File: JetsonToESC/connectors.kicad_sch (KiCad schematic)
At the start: 7 parts, among them J1 Conn_01x12, J2 Conn_01x03, J3 Conn_01x02

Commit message: Start On this Branch
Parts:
- added U4: MCP23018x-x-SS, Package_SO:SSOP-24_5.3x8.2mm_P0.65mm, symbol Interface_Expansion:MCP23018x-x-SS
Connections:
- net 5V: now also U4.10 (V_{DD})
- net BUTTON_100%: now also U4.22 (GPA5)
- net BUTTON_25%: now also U4.19 (GPA2)
- net BUTTON_50%: now also U4.20 (GPA3)
- net BUTTON_75%: now also U4.21 (GPA4)
- net BUTTON_STOP: now also U4.18 (GPA1)
- net GND: now also U4.1 (V_{SS})
- net LED_BATT_HI: now also U4.7 (GPB5)
- net LED_BATT_LOW: now also U4.9 (GPB7)
- net LED_BATT_MED: now also U4.8 (GPB6)
- net LED_OVERCURRENT: now also U4.5 (GPB3), U4.6 (GPB4)
- new net I2C_SCL: U4.11 (SCL)
- new net I2C_SDA: U4.12 (SDA)
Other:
- moved on the sheet: H1, H2, H3, H4, J1, J2, J3

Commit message: Work on current sense and io expansion branch
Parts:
- removed U4: MCP23018x-x-SS, Package_SO:SSOP-24_5.3x8.2mm_P0.65mm, symbol Interface_Expansion:MCP23018x-x-SS
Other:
- moved on the sheet: J1, J2, J3

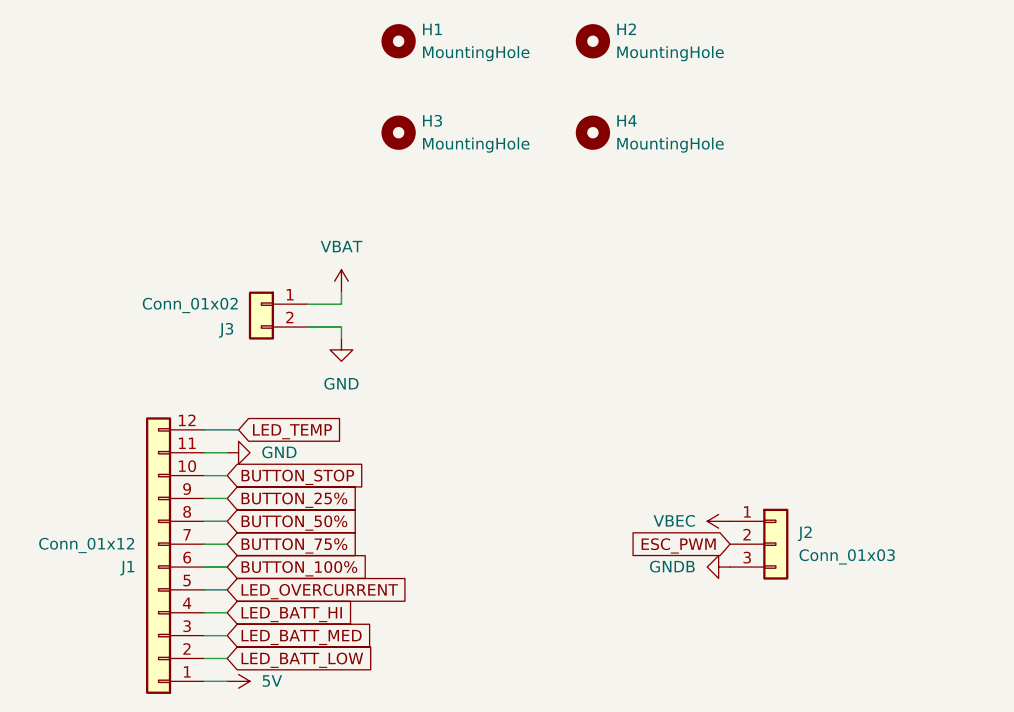
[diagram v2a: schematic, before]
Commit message: Updated routing for IO Expander and Hall Sensor
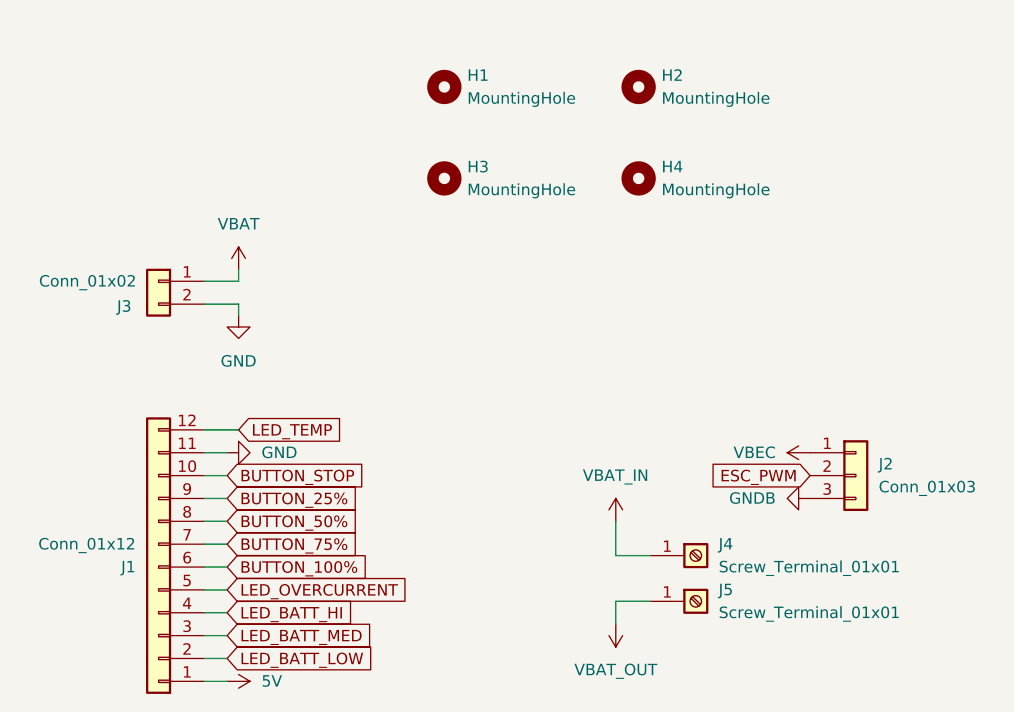
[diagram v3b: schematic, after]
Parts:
- added J4, J5: Screw_Terminal_01x01, MountingHole:MountingHole_4.3mm_M4_Pad_Via, symbol Connector:Screw_Terminal_01x01
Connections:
- new net VBAT_IN: J4.1 (Pin_1)
- new net VBAT_OUT: J5.1 (Pin_1)
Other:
- moved on the sheet: H1, H2, H3, H4, J2, J3

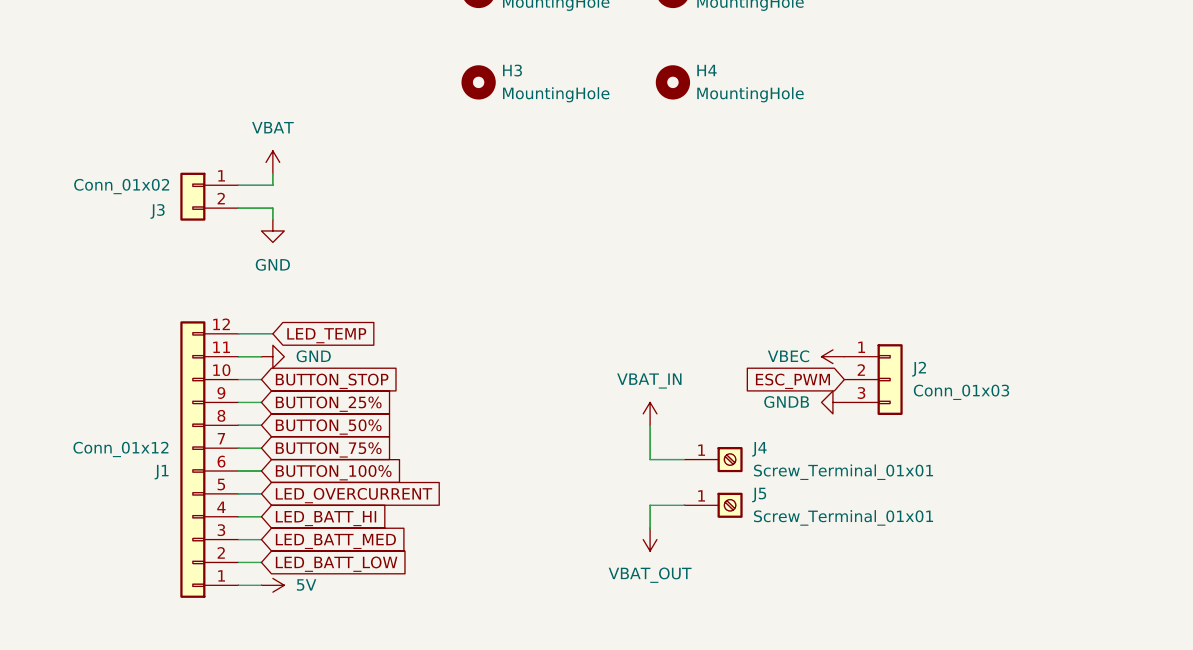
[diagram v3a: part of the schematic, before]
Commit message: Design almost finished, added vias array for grounding too
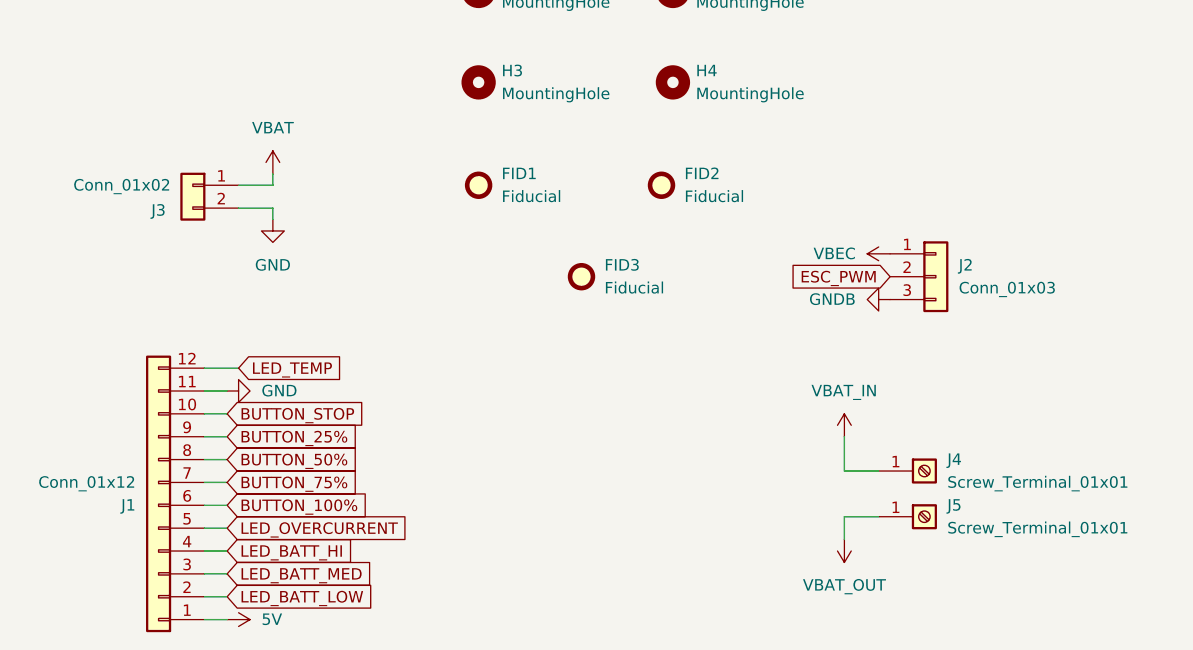
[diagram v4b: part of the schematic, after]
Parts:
- added FID1, FID2, FID3: Fiducial, Fiducial:Fiducial_0.5mm_Mask1.5mm, symbol Mechanical:Fiducial
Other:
- moved on the sheet: J1, J2, J4, J5

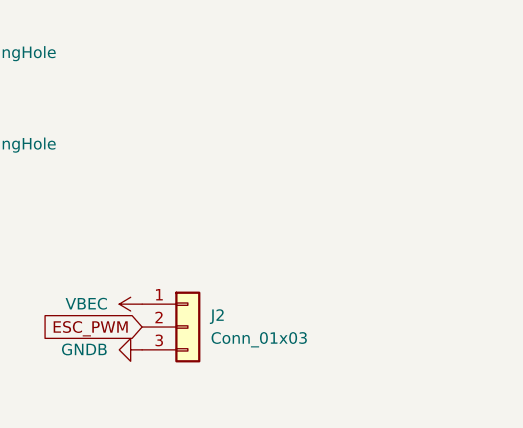
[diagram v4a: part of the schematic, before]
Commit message: Design almost finished, added vias array for grounding too
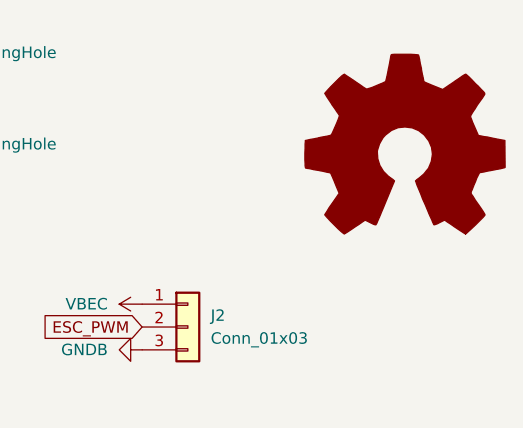
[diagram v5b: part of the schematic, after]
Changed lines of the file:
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@@
+	)
+	(symbol
+		(lib_id "Graphic:Logo_Open_Hardware_Large")
+		(at 170.18 36.83 0)
+		(unit 1)
+		(exclude_from_sim no)
+		(in_bom no)
+		(on_board no)
+		(dnp no)
+		(fields_autoplaced yes)
+		(property "Reference" "#SYM1"
+			(at 170.18 24.13 0)
+			(effects
+				(font
+					(size 1.27 1.27)
+				)
+				(hide yes)
+			)
+		)
+		(property "Value" "Logo_Open_Hardware_Large"
+			(at 170.18 46.99 0)
+			(effects
+				(font
+					(size 1.27 1.27)
+				)
+				(hide yes)
+			)
+		)
+		(property "Footprint" "Symbol:OSHW-Logo_28.5x30mm_SilkScreen"
+			(at 170.18 36.83 0)
+			(effects
+				(font
+					(size 1.27 1.27)
+				)
+				(hide yes)
+			)
+		)
+		(property "Datasheet" "~"
+			(at 170.18 36.83 0)
+			(effects
+				(font
+					(size 1.27 1.27)
+				)
+				(hide yes)
+			)
+		)
+		(property "Description" "Open Hardware logo, large"
+			(at 170.18 36.83 0)
+			(effects
+				(font
+					(size 1.27 1.27)
+				)
+				(hide yes)
+			)
+		)
+		(property "Sim.Enable" "0"
+			(at 170.18 36.83 0)
+			(effects
+				(font
+					(size 1.27 1.27)
+				)
+				(hide yes)
+			)
+		)
+		(instances
+			(project ""
+				(path "/47af999a-55f7-4333-ac4c-b272b7fb2895/bd87f1de-e46c-4816-9460-8a924dc991a8"
+					(reference "#SYM1")
+					(unit 1)
+				)
+			)
+		)
 	)
 	(symbol

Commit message: Design and routing done
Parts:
- added MoaBoardsLogo1: ~, Logos:MoaBoards, symbol Logos:LogoMoaBoards
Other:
- moved on the sheet: FID1, FID2, FID3, H1, H2, H3, H4, J1, J2, J3, J4, J5

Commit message: Updated for v2.0, almost complete
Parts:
- removed J2: Conn_01x03, Connector_JST:JST_EH_S3B-EH_1x03_P2.50mm_Horizontal, symbol Connector_Generic:Conn_01x03
- added J2: Conn_01x02, Connector_JST:JST_EH_S2B-EH_1x02_P2.50mm_Horizontal, symbol Connector_Generic:Conn_01x02
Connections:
- net ESC_PWM: now also J2.1 (Pin_1)
- net GNDB: now also J2.2 (Pin_2)
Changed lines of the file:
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@@
-	)
-	(symbol
-		(lib_id "power:VCC")
-		(at 144.78 55.88 90)
-		(unit 1)
-		(exclude_from_sim no)
-		(in_bom yes)
-		(on_board yes)
-		(dnp no)
-		(fields_autoplaced yes)
-		(property "Reference" "#PWR012"
-			(at 148.59 55.88 0)
-			(effects
-				(font
-					(size 1.27 1.27)
-				)
-				(hide yes)
-			)
-		)
-		(property "Value" "VBEC"
-			(at 140.97 55.8799 90)
-			(effects
-				(font
-					(size 1.27 1.27)
-				)
-				(justify left)
-			)
-		)
-		(property "Footprint" ""
-			(at 144.78 55.88 0)
-			(effects
-				(font
-					(size 1.27 1.27)
-				)
-				(hide yes)
-			)
-		)
-		(property "Datasheet" ""
-			(at 144.78 55.88 0)
-			(effects
-				(font
-					(size 1.27 1.27)
-				)
-				(hide yes)
-			)
-		)
-		(property "Description" "Power symbol creates a global label with name \"VCC\""
-			(at 144.78 55.88 0)
-			(effects
-				(font
-					(size 1.27 1.27)
-				)
-				(hide yes)
-			)
-		)
-		(pin "1"
-		)
-		(instances
-			(project "JetsonToESC"
-				(path "/47af999a-55f7-4333-ac4c-b272b7fb2895/bd87f1de-e46c-4816-9460-8a924dc991a8"
-					(reference "#PWR012")
-					(unit 1)
-				)
-			)
-		)
 	)
 	(symbol
@@
 	)
 	(symbol
+		(lib_id "Connector_Generic:Conn_01x02")
+		(at 149.86 58.42 0)
+		(unit 1)
+		(exclude_from_sim no)
+		(in_bom yes)
+		(on_board yes)
+		(dnp no)
+		(property "Reference" "J2"
+			(at 153.67 61.214 0)
+			(effects
+				(font
+					(size 1.27 1.27)
+				)
+			)
+		)
+		(property "Value" "Conn_01x02"
+			(at 157.734 58.42 0)
+			(effects
+				(font
+					(size 1.27 1.27)
+				)
+			)
+		)
+		(property "Footprint" "Connector_JST:JST_EH_S2B-EH_1x02_P2.50mm_Horizontal"
+			(at 149.86 58.42 0)
+			(effects
+				(font
+					(size 1.27 1.27)
+				)
+				(hide yes)
+			)
+		)
+		(property "Datasheet" "~"
+			(at 149.86 58.42 0)
+			(effects
+				(font
+					(size 1.27 1.27)
+				)
+				(hide yes)
+			)
+		)
+		(property "Description" "Generic connector, single row, 01x02, script generated (kicad-library-utils/schlib/autogen/connector/)"
+			(at 149.86 58.42 0)
+			(effects
+				(font
+					(size 1.27 1.27)
+				)
+				(hide yes)
+			)
+		)
+		(pin "2"
+		)
+		(pin "1"
+		)
+		(instances
+			(project "JetsonToESC"
+				(path "/47af999a-55f7-4333-ac4c-b272b7fb2895/bd87f1de-e46c-4816-9460-8a924dc991a8"
+					(reference "J2")
+					(unit 1)
+				)
+			)
+		)
+	)
+	(symbol
 		(lib_id "power:VCC")
 		(at 55.88 41.91 0)
@@
 					(unit 1)
 				)
-			)
-		)
-	)
-	(symbol
-		(lib_id "Connector_Generic:Conn_01x03")
-		(at 149.86 58.42 0)
-		(unit 1)
-		(exclude_from_sim no)
-		(in_bom yes)
-		(on_board yes)
-		(dnp no)
-		(property "Reference" "J2"
-			(at 152.4 57.1499 0)
-			(effects
-				(font
-					(size 1.27 1.27)
-				)
-				(justify left)
-			)
-		)
-		(property "Value" "Conn_01x03"
-			(at 152.4 59.6899 0)
-			(effects
-				(font
-					(size 1.27 1.27)
-				)
-				(justify left)
-			)
-		)
-		(property "Footprint" "Connector_JST:JST_EH_S3B-EH_1x03_P2.50mm_Horizontal"
-			(at 149.86 58.42 0)
-			(effects
-				(font
-					(size 1.27 1.27)
-				)
-				(hide yes)
-			)
-		)
-		(property "Datasheet" "~"
-			(at 149.86 58.42 0)
-			(effects
-				(font
-					(size 1.27 1.27)
-				)
-				(hide yes)
-			)
-		)
-		(property "Description" "Generic connector, single row, 01x03, script generated (kicad-library-utils/schlib/autogen/connector/)"
-			(at 149.86 58.42 0)
-			(effects
-				(font
-					(size 1.27 1.27)
-				)
-				(hide yes)
-			)
-		)
-		(pin "2"
-		)
-		(pin "1"
-		)
-		(pin "3"
-		)
-		(instances
-			(project "JetsonToESC"
-				(path "/47af999a-55f7-4333-ac4c-b272b7fb2895/bd87f1de-e46c-4816-9460-8a924dc991a8"
-					(reference "J2")
-					(unit 1)
-				)

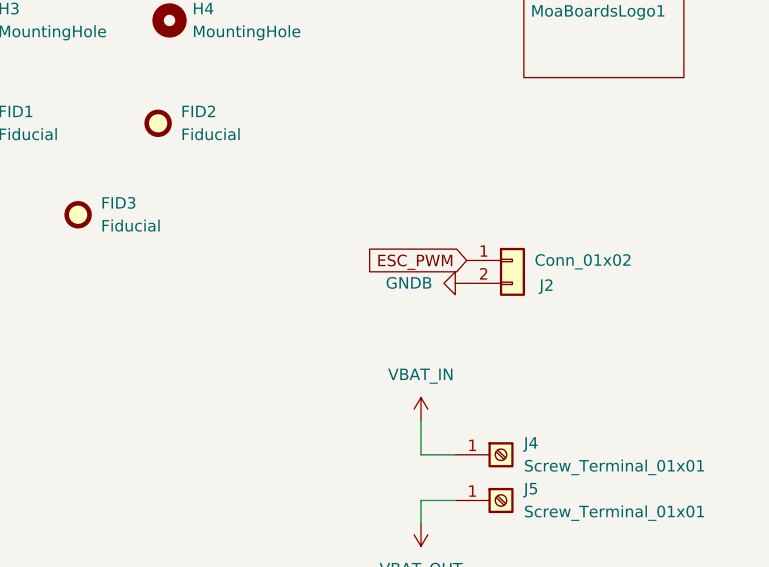
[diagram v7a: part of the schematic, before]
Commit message: Changing connectors from JST to Generic male 2.54mm headers
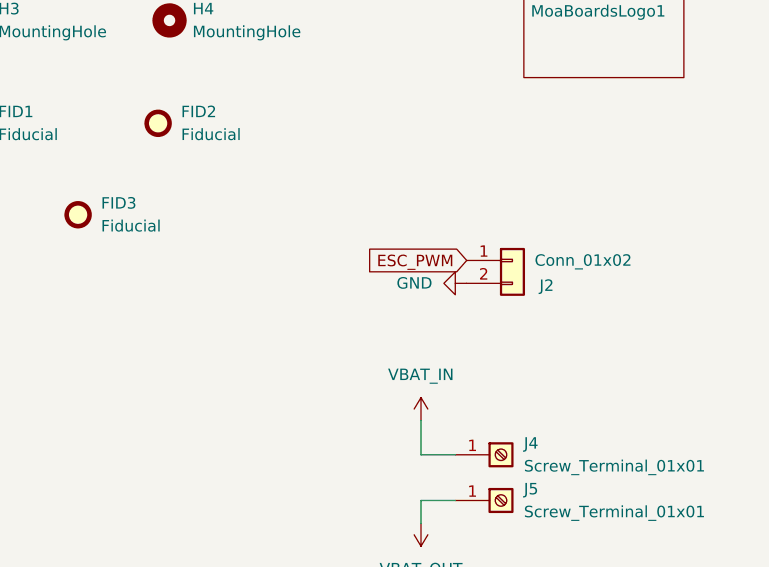
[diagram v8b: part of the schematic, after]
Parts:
- J1: footprint Connector_JST:JST_EH_S12B-EH_1x12_P2.50mm_Horizontal -> Connector_PinHeader_2.54mm:PinHeader_1x12_P2.54mm_Horizontal
- J2, J3: footprint Connector_JST:JST_EH_S2B-EH_1x02_P2.50mm_Horizontal -> Connector_PinHeader_2.54mm:PinHeader_1x02_P2.54mm_Horizontal
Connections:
- net GNDB is gone; now on net GND: J2.2 (Pin_2)
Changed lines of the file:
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@@
 		)
 		(instances
-			(project ""
+			(project "JetsonToESC"
 				(path "/47af999a-55f7-4333-ac4c-b272b7fb2895/bd87f1de-e46c-4816-9460-8a924dc991a8"
 					(reference "FID1")
@@
 			)
 		)
-		(property "Footprint" "Connector_JST:JST_EH_S2B-EH_1x02_P2.50mm_Horizontal"
+		(property "Footprint" "Connector_PinHeader_2.54mm:PinHeader_1x02_P2.54mm_Horizontal"
 			(at 46.99 43.18 0)
 			(effects
@@
 			)
 		)
-		(property "Value" "GNDB"
+		(property "Value" "GND"
 			(at 140.97 60.9599 90)
 			(effects
@@
 			)
 		)
-		(property "Footprint" "Connector_JST:JST_EH_S2B-EH_1x02_P2.50mm_Horizontal"
+		(property "Footprint" "Connector_PinHeader_2.54mm:PinHeader_1x02_P2.54mm_Horizontal"
 			(at 149.86 58.42 0)
 			(effects
@@
 		)
 		(instances
-			(project ""
+			(project "JetsonToESC"
 				(path "/47af999a-55f7-4333-ac4c-b272b7fb2895/bd87f1de-e46c-4816-9460-8a924dc991a8"
 					(reference "MoaBoardsLogo1")
@@
 		)
 		(instances
-			(project ""
+			(project "JetsonToESC"
 				(path "/47af999a-55f7-4333-ac4c-b272b7fb2895/bd87f1de-e46c-4816-9460-8a924dc991a8"
 					(reference "J4")
@@
 			)
 		)
-		(property "Footprint" "Connector_JST:JST_EH_S12B-EH_1x12_P2.50mm_Horizontal"
+		(property "Footprint" "Connector_PinHeader_2.54mm:PinHeader_1x12_P2.54mm_Horizontal"
 			(at 43.18 78.74 0)
 			(effects
